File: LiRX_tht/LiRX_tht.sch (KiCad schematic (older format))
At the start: 38 parts, among them J1 TP8, J10 onoff, J11 TP9, J2 TP3, J3 TP4, J4 buchse, J5 TP2, J6 TP5, J7 TP7, J8 TP1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

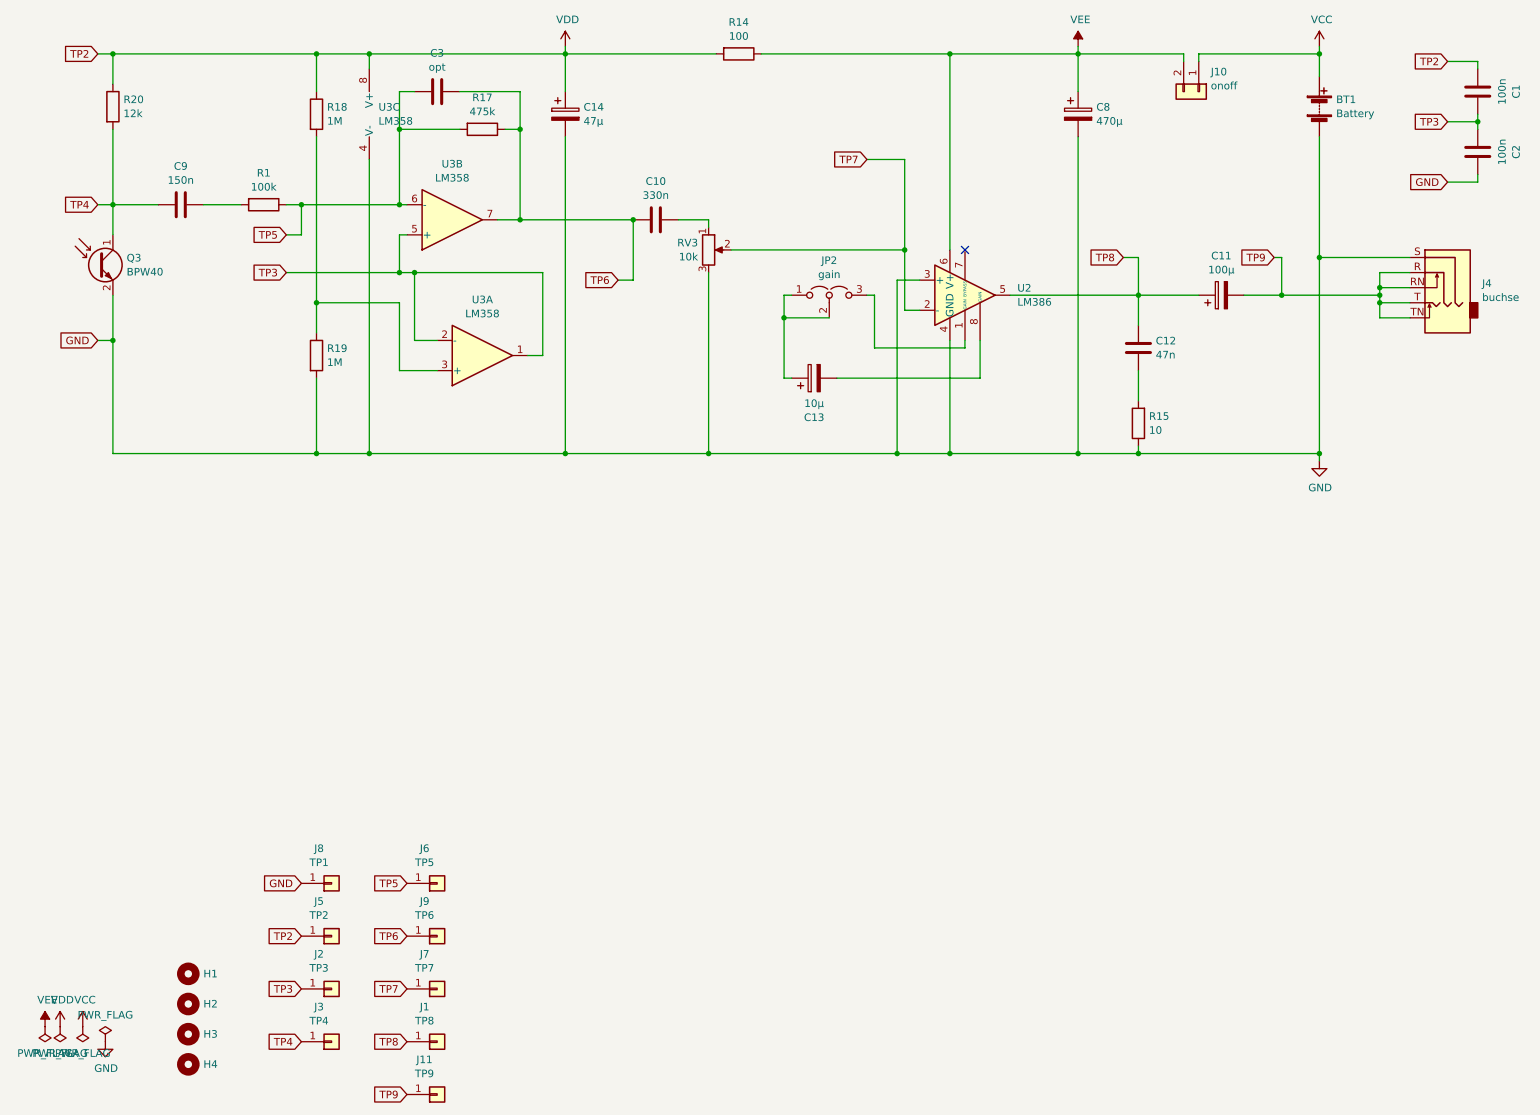
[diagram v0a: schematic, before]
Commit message: Added Suggestions; 1cm longer; kicad 6.0
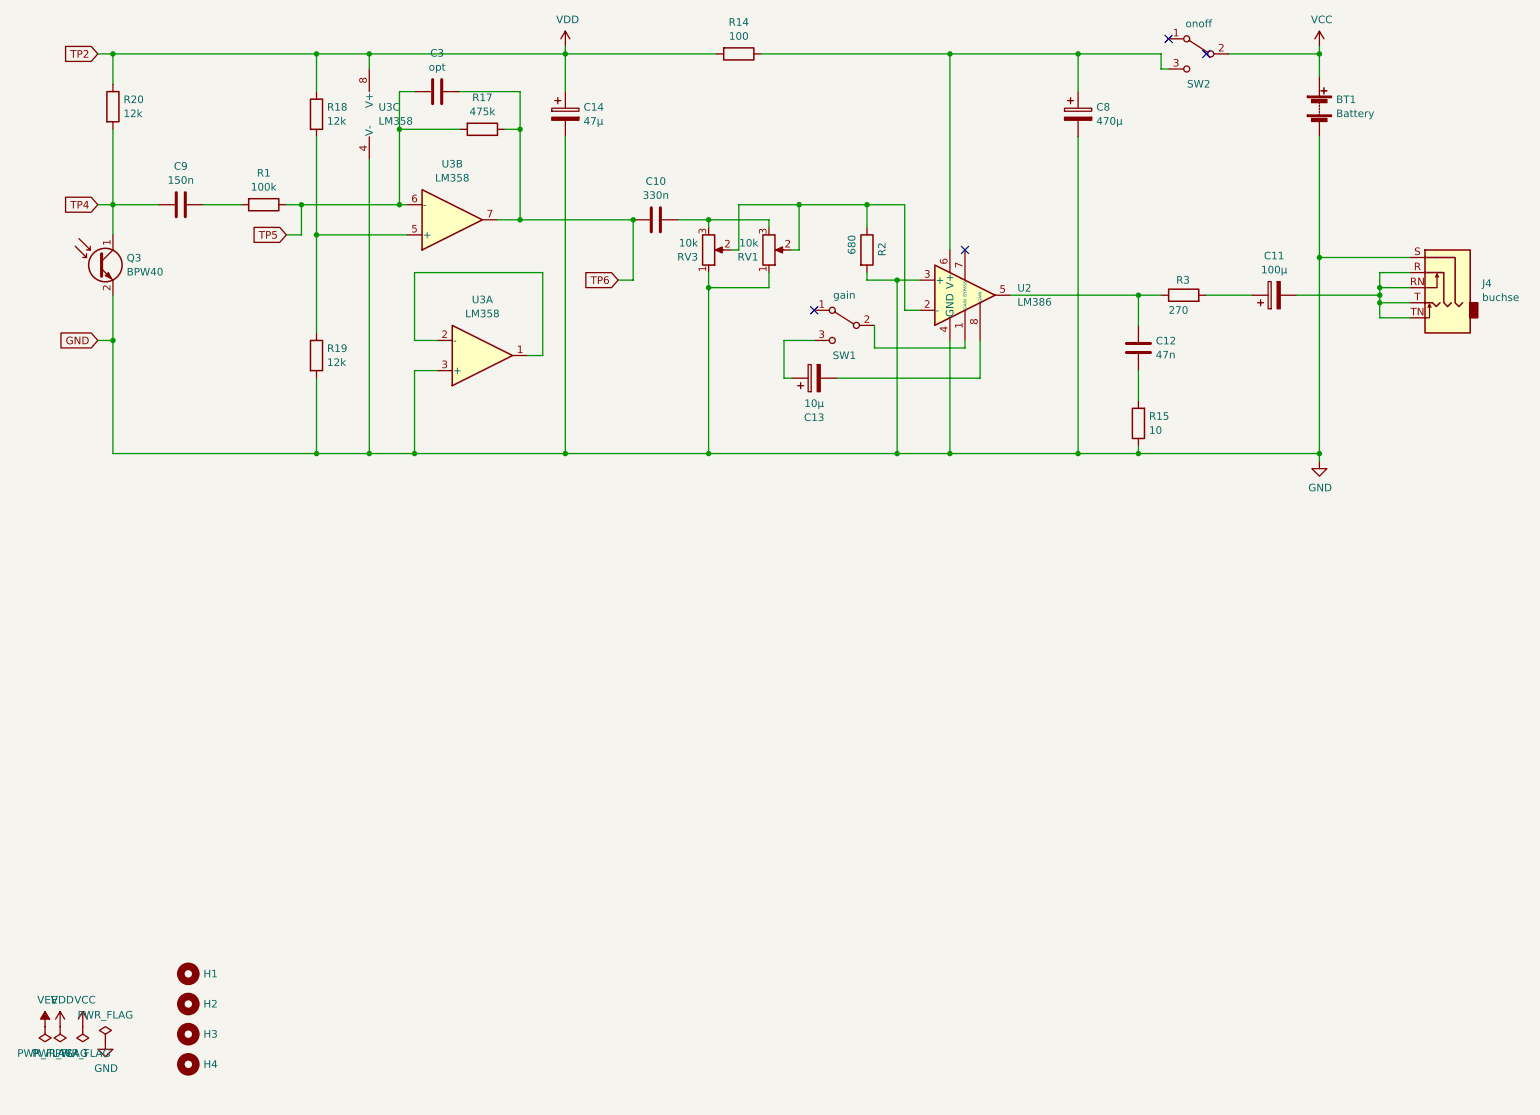
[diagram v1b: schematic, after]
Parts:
- removed C1, C2: 100n, Capacitor_THT:C_Disc_D3.0mm_W1.6mm_P2.50mm, symbol Device:C
- removed J1: TP8, Connector_PinHeader_1.27mm:PinHeader_1x01_P1.27mm_Vertical, symbol Connector_Generic:Conn_01x01
- removed J10: onoff, Connector_PinHeader_2.54mm:PinHeader_1x02_P2.54mm_Vertical, symbol Connector_Generic:Conn_01x02
- removed J11: TP9, Connector_PinHeader_1.27mm:PinHeader_1x01_P1.27mm_Vertical, symbol Connector_Generic:Conn_01x01
- removed J2: TP3, Connector_PinHeader_1.27mm:PinHeader_1x01_P1.27mm_Vertical, symbol Connector_Generic:Conn_01x01
- removed J3: TP4, Connector_PinHeader_1.27mm:PinHeader_1x01_P1.27mm_Vertical, symbol Connector_Generic:Conn_01x01
- removed J5: TP2, Connector_PinHeader_1.27mm:PinHeader_1x01_P1.27mm_Vertical, symbol Connector_Generic:Conn_01x01
- removed J6: TP5, Connector_PinHeader_1.27mm:PinHeader_1x01_P1.27mm_Vertical, symbol Connector_Generic:Conn_01x01
- removed J7: TP7, Connector_PinHeader_1.27mm:PinHeader_1x01_P1.27mm_Vertical, symbol Connector_Generic:Conn_01x01
- removed J8: TP1, Connector_PinHeader_1.27mm:PinHeader_1x01_P1.27mm_Vertical, symbol Connector_Generic:Conn_01x01
- removed J9: TP6, Connector_PinHeader_1.27mm:PinHeader_1x01_P1.27mm_Vertical, symbol Connector_Generic:Conn_01x01
- removed JP2: gain, Connector_PinHeader_2.54mm:PinHeader_1x03_P2.54mm_Vertical, symbol Jumper:Jumper_3_Open
- added R2: 680, Resistor_THT:R_Axial_DIN0207_L6.3mm_D2.5mm_P2.54mm_Vertical, symbol Device:R
- added R3: 270, Resistor_THT:R_Axial_DIN0207_L6.3mm_D2.5mm_P2.54mm_Vertical, symbol Device:R
- added RV1: 10k, Potentiometer_THT:Potentiometer_Piher_T-16H_Single_Horizontal, symbol Device:R_POT
- added SW1: gain, Button_Switch_THT:SW_CuK_OS102011MA1QN1_SPDT_Angled, symbol Switch:SW_SPDT
- added SW2: onoff, Button_Switch_THT:SW_CuK_OS102011MA1QN1_SPDT_Angled, symbol Switch:SW_SPDT
- C10, C9: footprint Capacitor_THT:C_Disc_D3.0mm_W1.6mm_P2.50mm -> Capacitor_THT:C_Rect_L7.0mm_W3.5mm_P2.50mm_P5.00mm
- C8: footprint Capacitor_THT:CP_Radial_D8.0mm_P3.50mm -> Capacitor_THT:CP_Radial_D10.0mm_P2.50mm_P5.00mm
- R1, R17, R20: footprint Resistor_THT:R_Axial_DIN0204_L3.6mm_D1.6mm_P7.62mm_Horizontal -> Resistor_THT:R_Axial_DIN0207_L6.3mm_D2.5mm_P10.16mm_Horizontal
- R14, R15: footprint Resistor_THT:R_Axial_DIN0204_L3.6mm_D1.6mm_P7.62mm_Horizontal -> Resistor_THT:R_Axial_DIN0207_L6.3mm_D2.5mm_P2.54mm_Vertical
- R18, R19: value 1M -> 12k; footprint Resistor_THT:R_Axial_DIN0204_L3.6mm_D1.6mm_P7.62mm_Horizontal -> Resistor_THT:R_Axial_DIN0207_L6.3mm_D2.5mm_P10.16mm_Horizontal
- RV3: footprint Potentiometer_THT:Potentiometer_Piher_T-16H_Single_Horizontal -> Potentiometer_THT:Potentiometer_Piher_PC-16_Single_Horizontal
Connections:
- net GND: now also RV3.1, U3.3 (+), R2.2, RV1.1; no longer RV3.3
- net VCC: now also SW2.2 (B)
- net VEE: no longer C8.1, R14.1, U2.6 (V+)
- net at R18.2, R19.1: now also U3.5 (+); no longer U3.3 (+)
- net at C10.1: now also RV3.3, RV1.3; no longer RV3.1
- net at C13.1: now also SW1.3 (C)
- net at U2.1 (GAIN): now also SW1.2 (B)
- net TP3: no longer names the net of U3.1, U3.2 (-)
- net TP3: no longer U3.5 (+)
- net TP7: no longer names the net of RV3.2, U2.2 (-)
- net TP7: now also R2.1, RV1.2
- net TP8: no longer names the net of C12.1, U2.5
- net TP8: now also R3.1; no longer C11.1
- net TP9: no longer names the net of C11.2, J4.R, J4.RN, J4.T, J4.TN
- new net: C8.1, R14.1, SW2.3 (C), U2.6 (V+)
- new net: C11.1, R3.2
- no-connect marks 1 -> 4
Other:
- moved on the sheet: C11
